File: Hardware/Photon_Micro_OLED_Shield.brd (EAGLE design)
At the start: 55.9 x 35.6 mm, 28 parts

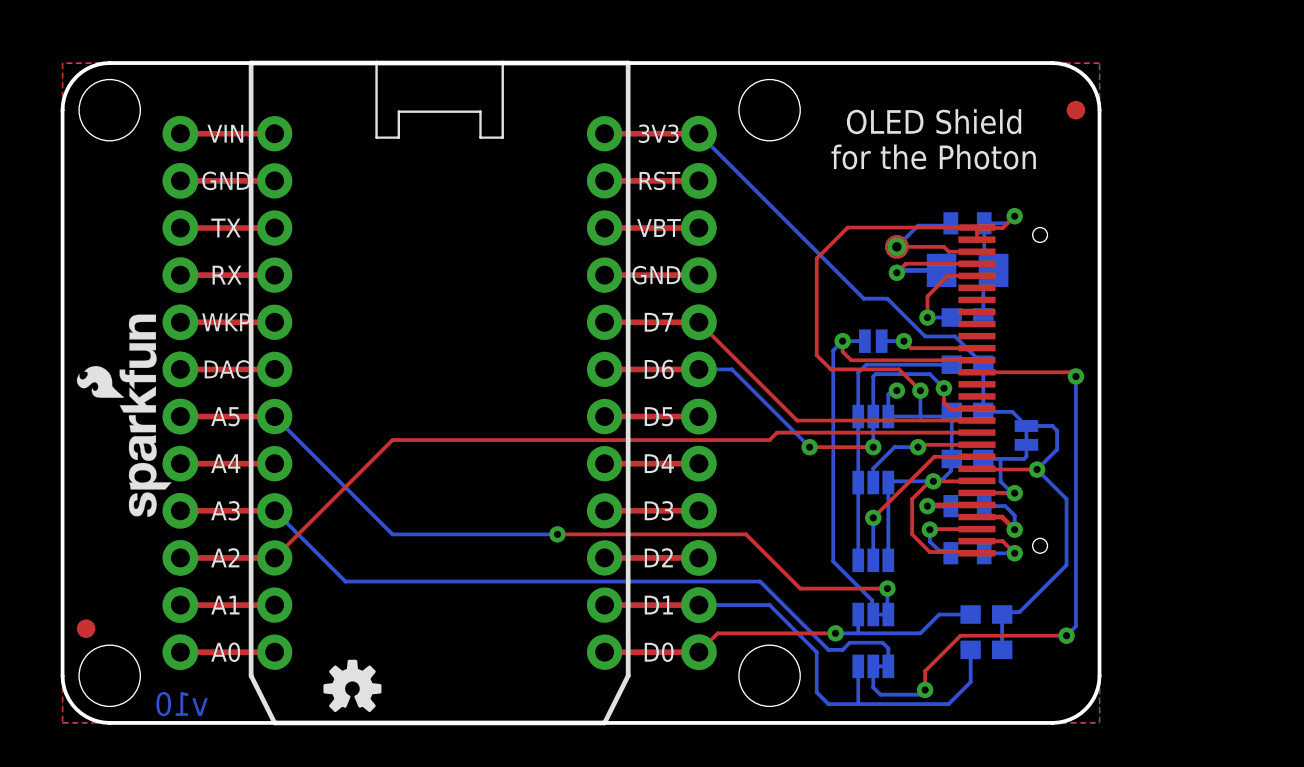
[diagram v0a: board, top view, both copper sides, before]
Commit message: Changes per design review (right place)
Board width fixed to allow space for headers and OLED screen.
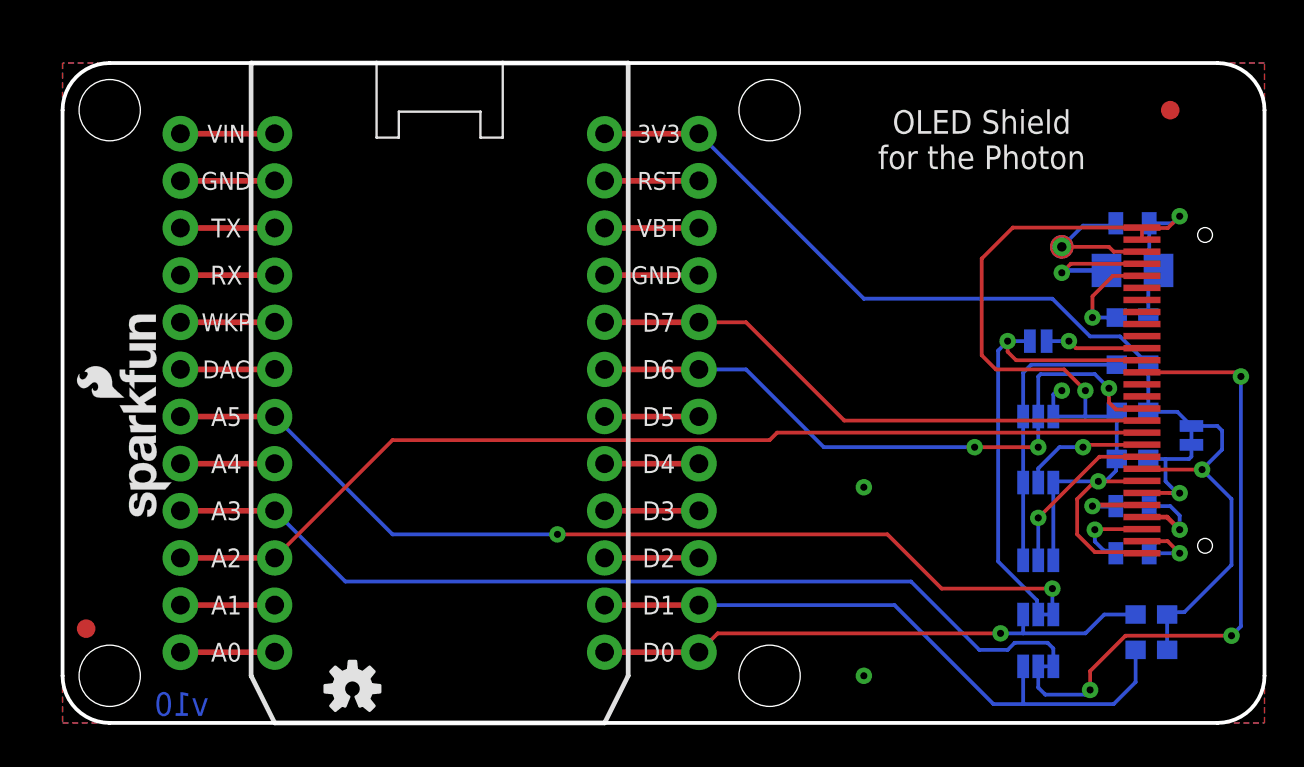
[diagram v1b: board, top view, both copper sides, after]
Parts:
- moved C1 8.89 mm to (58.9, 25.7)
- moved C2 8.89 mm to (58.9, 10.4)
- moved C3 8.89 mm to (58.9, 7.87)
- moved C4 8.89 mm to (58.9, 15.5)
- moved C5 8.89 mm to (58.9, 23.1)
- moved C6 8.89 mm to (58.9, 13.0)
- moved OLED1 8.89 mm to (59.4, 7.87)
- moved R1 8.89 mm to (58.9, 20.6)
- moved R2 8.89 mm to (58.9, 18.0)
- moved R5 8.89 mm to (59.9, 4.57)
- moved R7 8.89 mm to (59.9, 2.67)
- moved SJ1 8.89 mm to (53.8, 7.49)
- moved SJ10 8.89 mm to (53.8, 1.78)
- moved SJ2 8.89 mm to (53.8, 11.7)
- moved SJ3 8.89 mm to (62.1, 14.2)
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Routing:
- net VDD: track 45.5 -> 54.4 mm
- net D6: track 21.8 -> 30.7 mm
- net SS: track 40.6 -> 49.5 mm
- net SCK: track 37.4 -> 46.3 mm
- net D7: track 17.2 -> 26.1 mm
- net D0/SDA: track 16.5 -> 25.4 mm
- net MOSI: track 38.5 -> 47.3 mm
- net D1/SCL: track 22.6 -> 30.2 mm
- net GND: vias 4 -> 6
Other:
- board size 55.9 x 35.6 mm -> 64.8 x 35.6 mm

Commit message: changed board name per new naming conventions
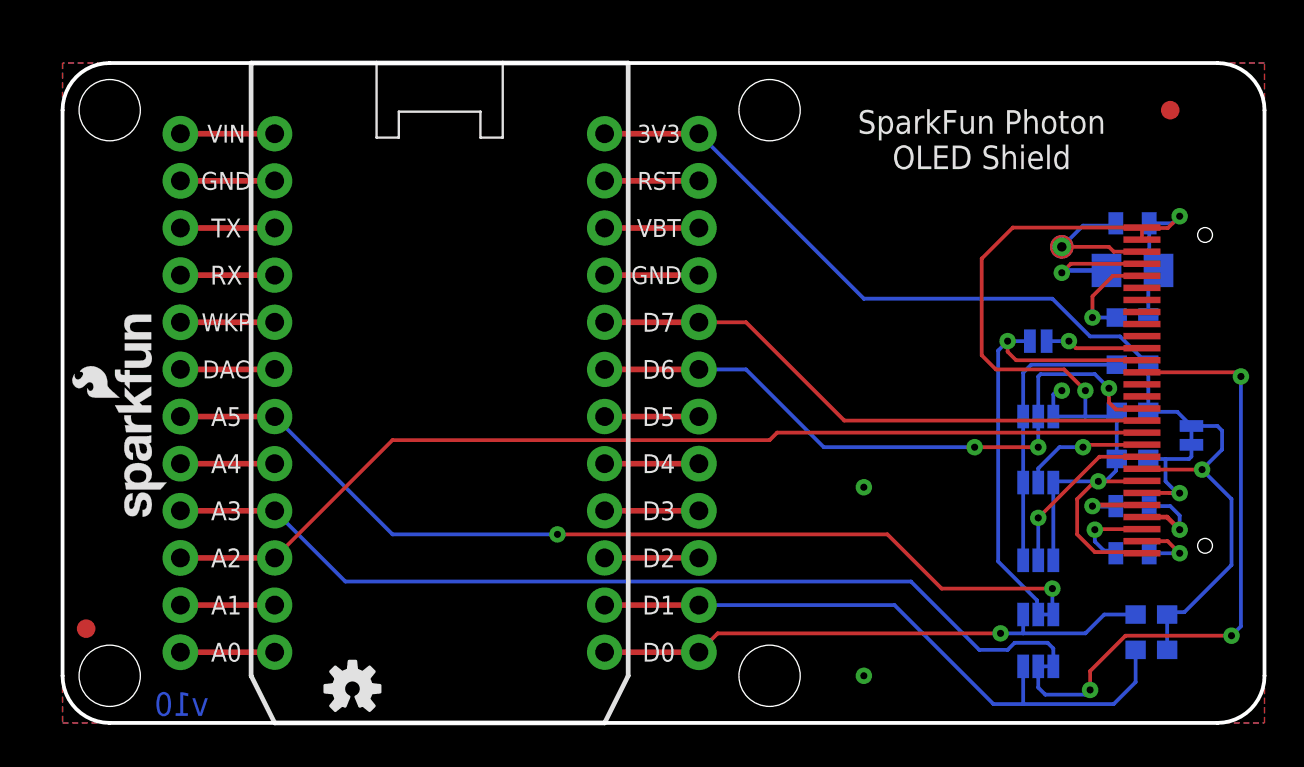
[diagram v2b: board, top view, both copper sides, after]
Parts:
- moved LOGO1 0.25 mm to (6.99, 9.40)
- moved LOGO2 0.13 mm to (6.99, 21.2)
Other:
- board text added: "SparkFun Photon OLED Shield"
- board text removed: "OLED Shield for the Photon"
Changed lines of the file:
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@@
 <dimension x1="6.35" y1="1.27" x2="4.699" y2="1.27" x3="5.5245" y3="-3.81" textsize="0.8128" textratio="15" layer="47" dtype="diameter" unit="inch" precision="3"/>
 <text x="3.81" y="-13.97" size="0.8128" layer="47" font="vector" ratio="15">Units in Inches</text>
-<text x="50.8" y="31.75" size="1.27" layer="21" font="vector" ratio="15" align="top-center">OLED Shield
-for the Photon</text>
+<text x="50.8" y="31.75" size="1.27" layer="21" font="vector" ratio="15" align="top-center">SparkFun Photon
+OLED Shield</text>
 <text x="51.943" y="4.191" size="0.8128" layer="22" font="vector" ratio="15" rot="MR0">SDA</text>
 <text x="58.166" y="4.191" size="0.8128" layer="22" font="vector" ratio="15" rot="MR0">MOSI</text>
@@
 <text x="57.658" y="1.27" size="0.8128" layer="22" font="vector" ratio="15" rot="MR0">SCK</text>
 <dimension x1="3.81" y1="-1.27" x2="66.04" y2="-1.27" x3="34.925" y3="-16.51" textsize="0.8128" textratio="15" layer="47" unit="inch"/>
-<text x="50.8" y="31.75" size="1.27" layer="22" font="vector" ratio="15" rot="MR0" align="top-center">OLED Shield
-for the Photon</text>
+<text x="50.8" y="31.75" size="1.27" layer="22" font="vector" ratio="15" rot="MR0" align="top-center">SparkFun Photon
+OLED Shield</text>
 </plain>
 <attributes>
@@
 <element name="SJ4" library="SparkFun-Passives" package="PAD-JUMPER-3-NO_YES_SILK" value="" x="53.848" y="15.24" rot="MR0"/>
 <element name="U$1" library="SparkFun-Aesthetics" package="SFE_LOGO_FLAME_.1" value="" x="17.907" y="-0.762" rot="MR0"/>
-<element name="LOGO1" library="SparkFun-Aesthetics" package="SFE_LOGO_NAME_FLAME_.1" value="SFE_LOGO_NAME_FLAME.1_INCH" x="7.239" y="9.398" rot="R90"/>
-<element name="LOGO2" library="SparkFun-Aesthetics" package="SFE_LOGO_NAME_FLAME_.1" value="SFE_LOGO_NAME_FLAME.1_INCH" x="7.112" y="21.209" rot="MR270"/>
+<element name="LOGO1" library="SparkFun-Aesthetics" package="SFE_LOGO_NAME_FLAME_.1" value="SFE_LOGO_NAME_FLAME.1_INCH" x="6.985" y="9.398" rot="R90"/>
+<element name="LOGO2" library="SparkFun-Aesthetics" package="SFE_LOGO_NAME_FLAME_.1" value="SFE_LOGO_NAME_FLAME.1_INCH" x="6.985" y="21.209" rot="MR270"/>
 </elements>
 <signals>

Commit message: Revising board name. Zero-ing origin, fixing measures.
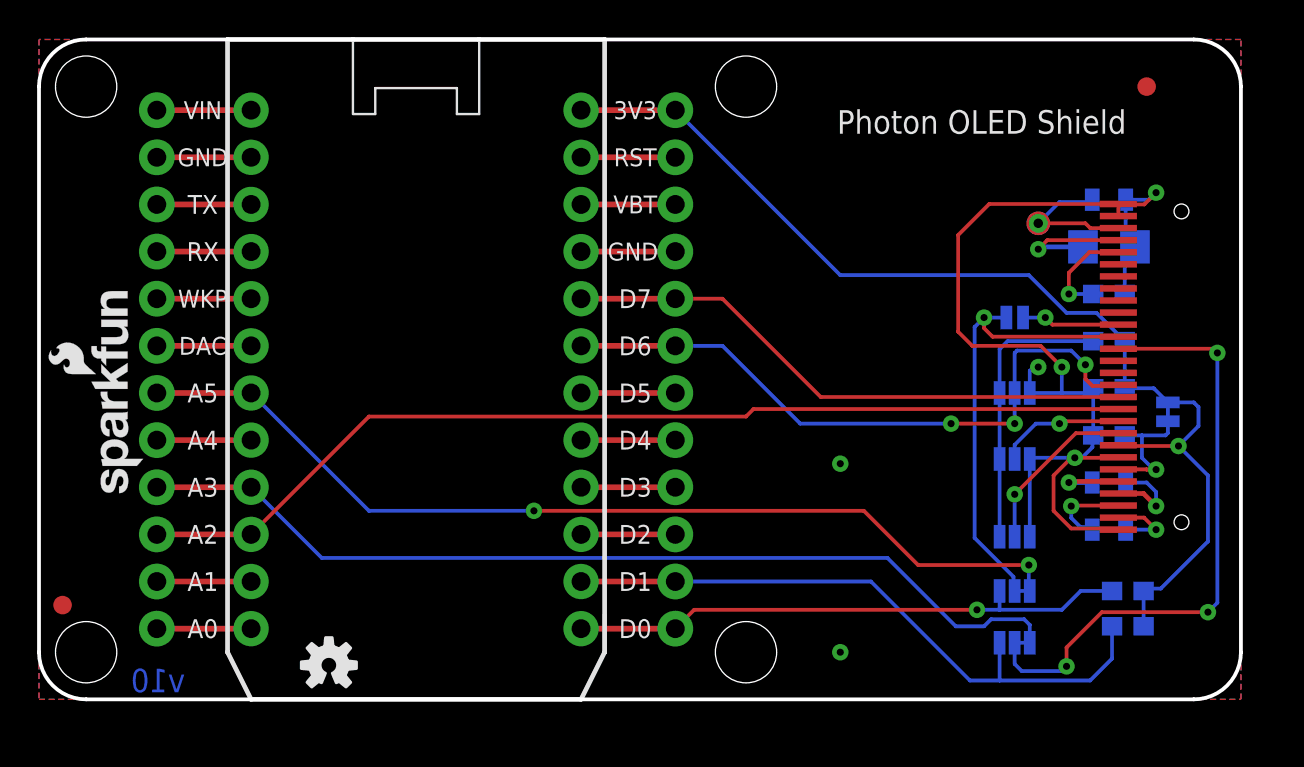
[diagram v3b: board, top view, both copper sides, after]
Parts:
- moved FRAME1 2.84 mm to (-1.27, -15.2)
- moved FID2 1.80 mm to (59.7, 33.0)
- moved OLED1 1.80 mm to (58.2, 9.14)
- moved R7 1.80 mm to (58.7, 3.94)
- moved R5 1.80 mm to (58.7, 5.84)
- moved SJ3 1.80 mm to (60.8, 15.5)
- moved TP1 1.80 mm to (53.8, 25.7)
- moved TP2 1.80 mm to (53.8, 25.7)
- moved FID1 1.80 mm to (1.27, 5.08)
- moved JP3 1.80 mm to (10.2, 0.00)
- moved LOGO1 1.80 mm to (5.71, 10.7)
- moved LOGO2 1.80 mm to (5.71, 22.5)
- moved U$1 1.80 mm to (16.6, 0.51)
- moved SJ5 1.80 mm to (52.6, 20.6)
- moved LOGO3 1.80 mm to (15.6, 1.84)
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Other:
- board text added: "Photon OLED Shield"
- board text removed: "SparkFun Photon OLED Shield"

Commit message: Updating silk. Bringing board edge in a bit.
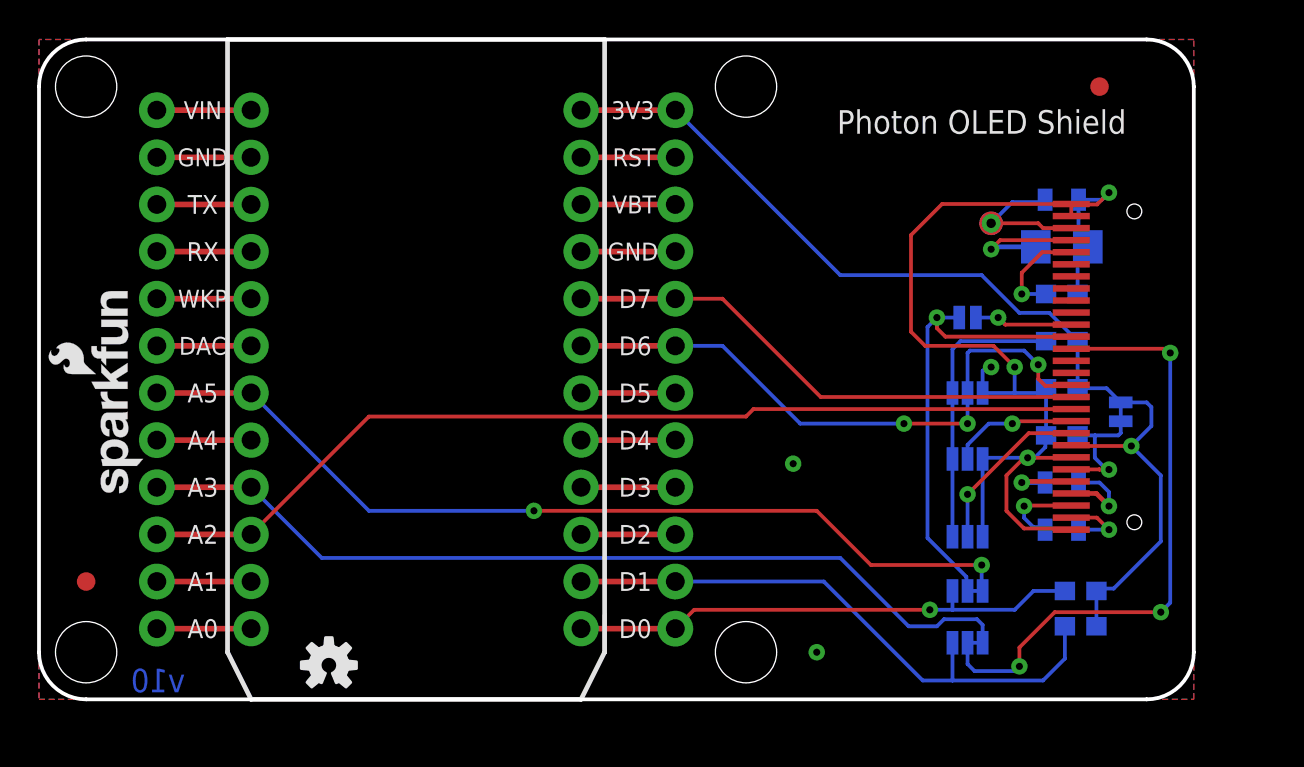
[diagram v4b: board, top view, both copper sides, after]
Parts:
- moved SJ1 2.54 mm to (50.0, 8.76)
- moved SJ10 2.54 mm to (50.0, 3.05)
- moved SJ2 2.54 mm to (50.0, 13.0)
- moved SJ4 2.54 mm to (50.0, 16.5)
- moved SJ5 2.54 mm to (50.0, 20.6)
- moved SJ8 2.54 mm to (50.0, 5.84)
- moved C1 2.54 mm to (55.1, 26.9)
- moved C2 2.54 mm to (55.1, 11.7)
- moved C3 2.54 mm to (55.1, 9.14)
- moved C4 2.54 mm to (55.1, 16.8)
- moved C5 2.54 mm to (55.1, 24.4)
- moved C6 2.54 mm to (55.1, 14.2)
- moved FID2 2.54 mm to (57.1, 33.0)
- moved OLED1 2.54 mm to (55.6, 9.14)
- moved R1 2.54 mm to (55.1, 21.8)
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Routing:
- net SS: track 49.5 -> 47.0 mm
- net D6: track 30.7 -> 28.2 mm
- net D1/SCL: track 30.2 -> 27.7 mm
- net SCK: track 46.3 -> 43.8 mm
- net MOSI: track 47.3 -> 44.8 mm
- net D7: track 26.1 -> 23.5 mm
- net D0/SDA: track 25.4 -> 22.9 mm
- net VDD: track 54.4 -> 51.8 mm
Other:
- board size 64.8 x 35.6 mm -> 62.2 x 35.6 mm

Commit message: issue fix
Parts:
- flipped FID1 to the bottom
- flipped FID2 to the bottom
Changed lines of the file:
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@@
 <attribute name="PROD_ID" value="RES-00824" x="55.118" y="19.304" size="1.778" layer="28" rot="MR180" display="off"/>
 </element>
-<element name="FID1" library="SparkFun-Aesthetics" package="FIDUCIAL-1X2" value="FIDUCIAL1X2" x="2.54" y="6.35" rot="R270"/>
-<element name="FID2" library="SparkFun-Aesthetics" package="FIDUCIAL-1X2" value="FIDUCIAL1X2" x="57.15" y="33.02" rot="R270"/>
+<element name="FID1" library="SparkFun-Aesthetics" package="FIDUCIAL-1X2" value="FIDUCIAL1X2" x="2.54" y="6.35" rot="MR270"/>
+<element name="FID2" library="SparkFun-Aesthetics" package="FIDUCIAL-1X2" value="FIDUCIAL1X2" x="57.15" y="33.02" rot="MR270"/>
 <element name="SJ5" library="SparkFun-Passives" package="PAD-JUMPER-2-NO_YES_SILK" value="" x="50.038" y="20.574" rot="MR180"/>
 <element name="TP1" library="SparkFun-Passives" package="PAD.03X.05" value="TEST-POINT3X5" x="51.308" y="25.654" rot="MR270"/>
